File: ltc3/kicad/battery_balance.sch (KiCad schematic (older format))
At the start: 41 parts, among them P701 BATT_MAIN, Q701 SUM110P08-11L, Q702 SUM110P08-11L, Q703 MMBT3904, U701 BQ77PL900

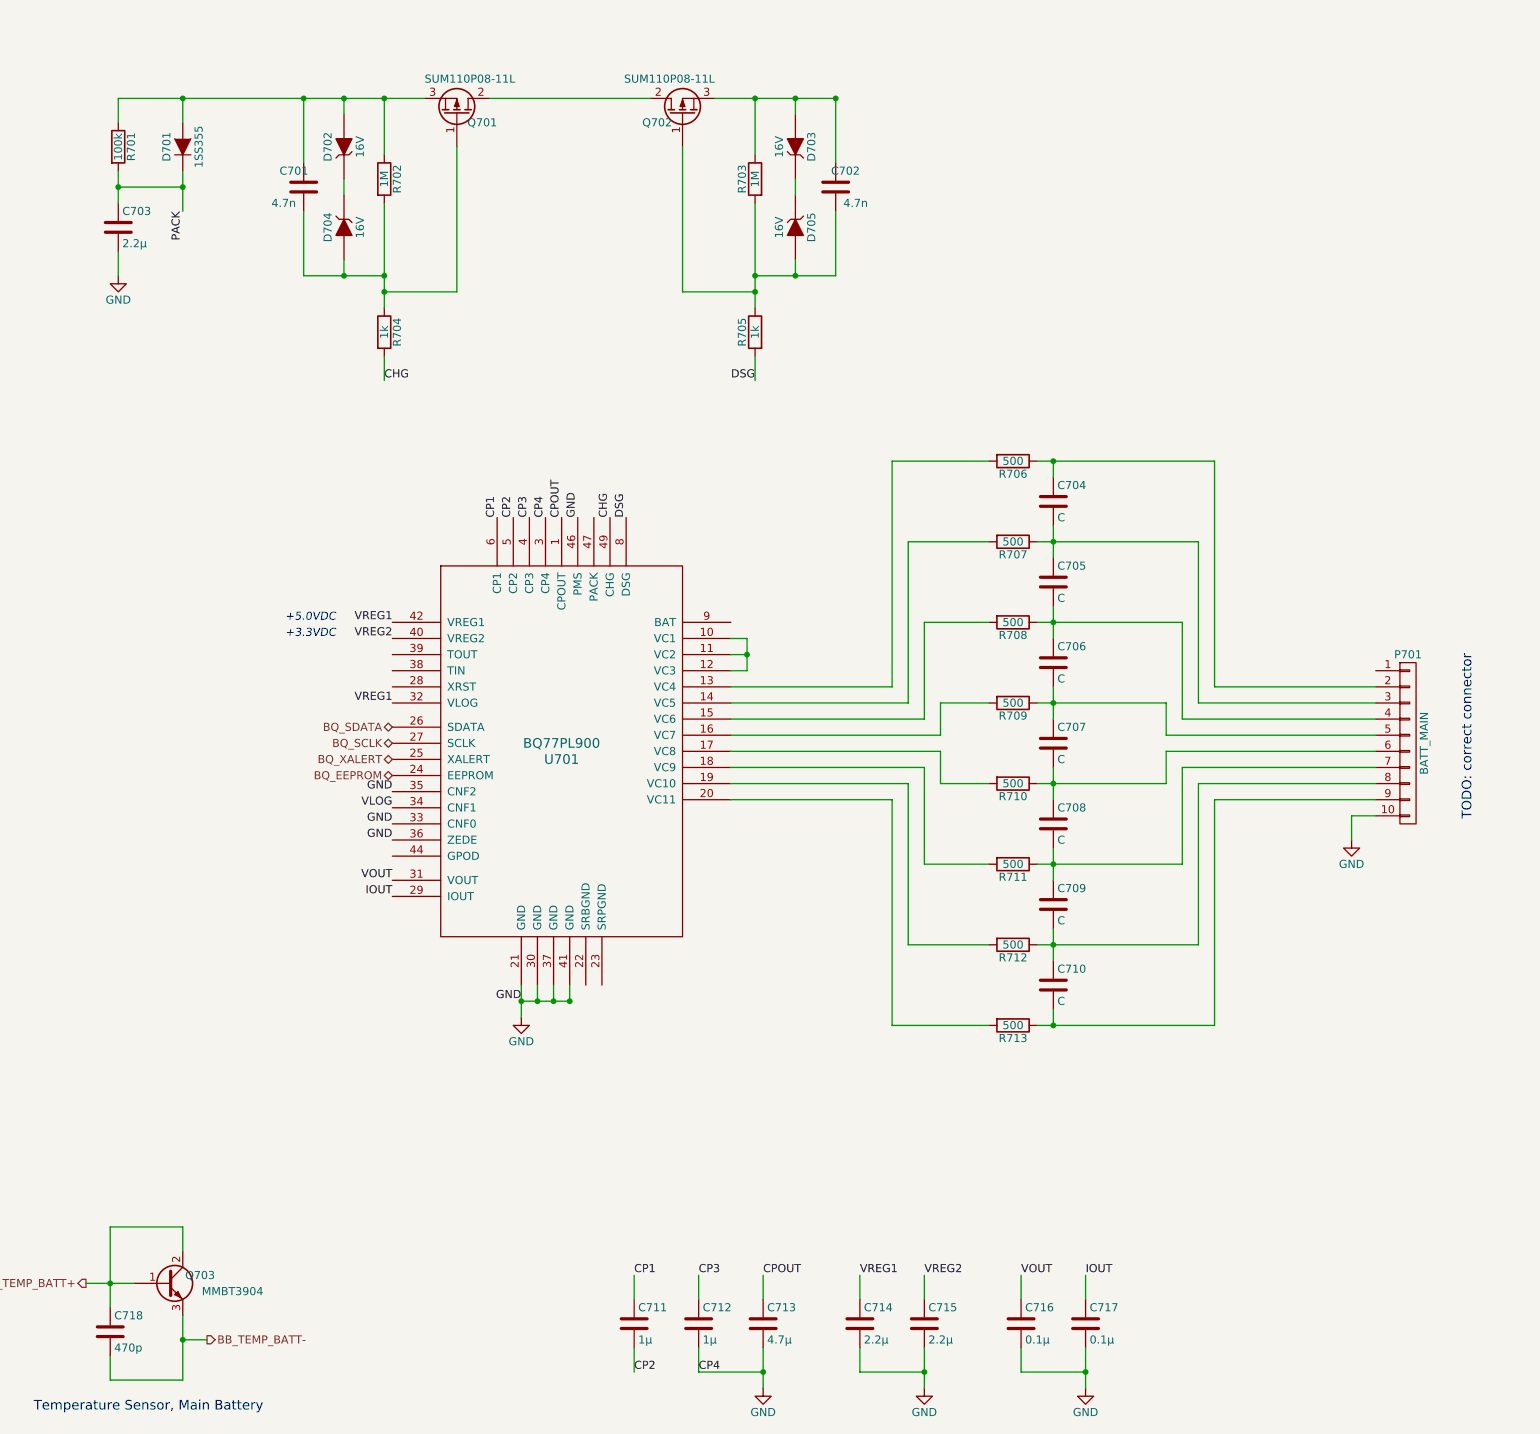
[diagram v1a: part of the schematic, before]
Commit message: LTC3: Reordered schematic sub-sheets; updated PDF export of schematic.
KiCad has an odd habit of ordering a schematic's sub-sheets without
notice.
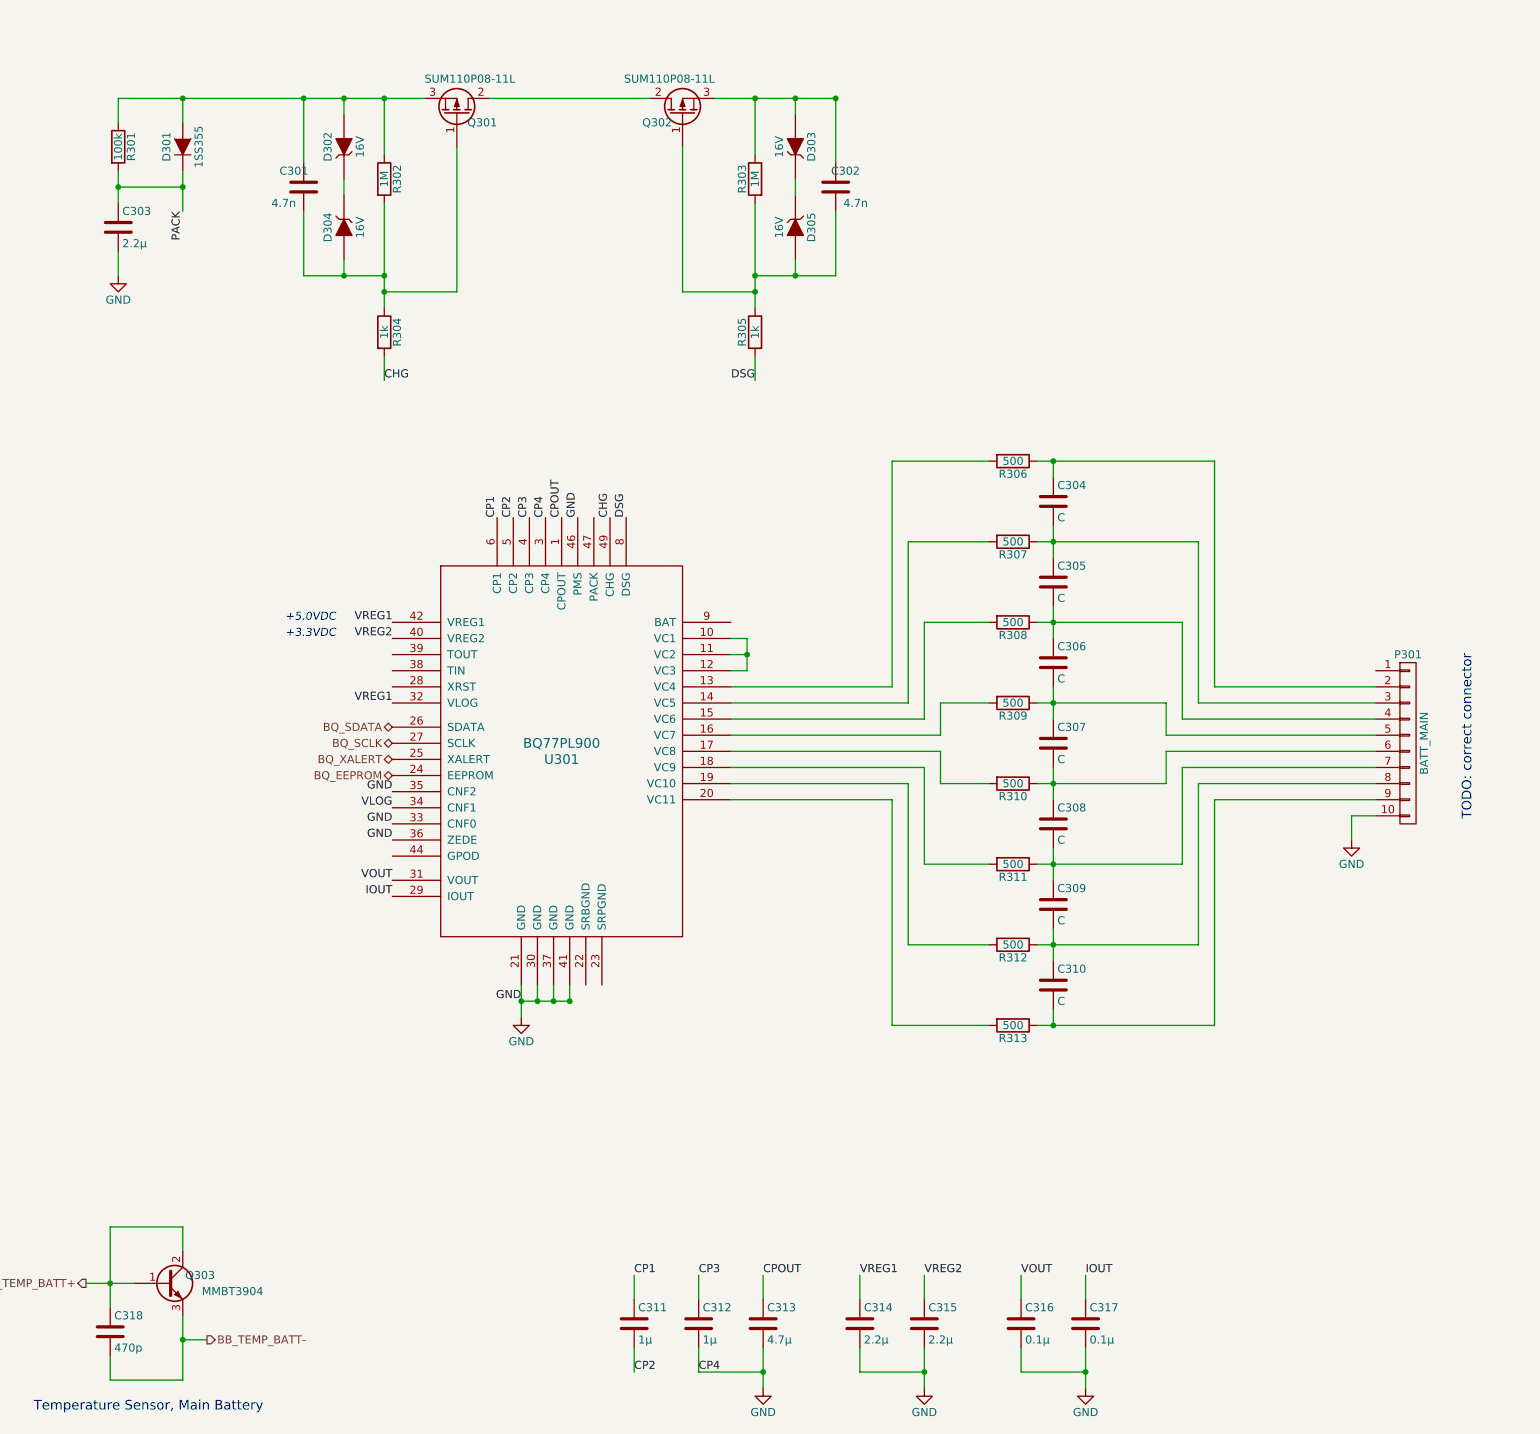
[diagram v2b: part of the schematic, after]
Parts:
- renumbered C701 to C301, C702 to C302, C703 to C303, C704 to C304, C705 to C305, C706 to C306, C707 to C307, C708 to C308, C709 to C309, C710 to C310, C711 to C311, C712 to C312, C713 to C313, C714 to C314, C715 to C315, C716 to C316, C717 to C317, C718 to C318, D701 to D301, D702 to D302, D703 to D303, D704 to D304, D705 to D305, P701 to P301, Q701 to Q301, Q702 to Q302, Q703 to Q303, R701 to R301, R702 to R302, R703 to R303, R704 to R304, R705 to R305, R706 to R306, R707 to R307, R708 to R308, R709 to R309, R710 to R310, R711 to R311, R712 to R312, R713 to R313, U701 to U301

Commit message: LTC3: Cleaned up I2C devices.
Gave each power sub-circuit its own LTC299x sensor.  Charger and
battery pack circuits each get an LTC2990 (quad); DC-DC converter
circuit gets an LTC2991 (octal).

Separate sensor ICs for each sub-circuit allows the chip to be as
close to its sense resistors as possible (and makes for a cleaner
schematic).
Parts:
- removed C318: 470p, symbol C
- removed P301: BATT_MAIN, symbol CONN_01X10
- removed Q303: MMBT3904, symbol Q_NPN_BCE
- added C?: 0.1μ, symbol C
- added C?: 470p, symbol C
- added P?: CONN_BATT_SENSE, symbol CONN_01X08
- added P?: CONN_BATT_MAIN, symbol CONN_01X02
- added Q?: MMBT3904, symbol Q_NPN_BCE
- added R?: R4T, symbol R4T
- added R?: 5k6, symbol R
- added U?: LTC2990, symbol LTC2990
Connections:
- net GND: now also C?.2, P?.2 (P2), U?.5 (GND), U?.9 (ADR1)
- net at U301.9 (BAT): now also C302.1, D303.2 (A), Q302.3 (S), R303.1, R?.2
- net at C304.1, R306.1: now also P?.1 (P1)
- net at C304.2, C305.1, R307.1: now also P?.2 (P2)
- net at C305.2, C306.1, R308.1: now also P?.3 (P3)
- net at C306.2, C307.1, R309.1: now also P?.4 (P4)
- net at C307.2, C308.1, R310.1: now also P?.5 (P5)
- net at C308.2, C309.1, R311.1: now also P?.6 (P6)
- net at C309.2, C310.1, R312.1: now also P?.7 (P7)
- net at C310.2, R313.1: now also P?.8 (P8)
- net VBATT: now reaches C301.1, D301.2 (A), D302.2 (A), Q301.3 (S), R301.1, R302.1
- net BQ_SCLK renamed I2C_CLOCK
- net I2C_CLOCK: now also U?.7 (SDL)
- net BQ_SDATA renamed I2C_DATA
- net I2C_DATA: now also U?.6 (SDA)
- net CHG: no longer names the net of R304.2, U301.49 (CHG)
- net DSG: no longer names the net of R305.2, U301.8 (DSG)
- new net: P?.1 (P1), R?.1
- new net: R?.4, U?.1 (V1)
- new net: R?.3, U?.2 (V2)
- new net: C?.1, Q?.1 (B), Q?.2 (C), U?.3 (V3)
- new net: C?.2, Q?.3 (E), U?.4 (V4)
- new net: R?.2, U?.8 (ADR0)
- new net +5V: C?.1, R?.1, U?.10 (Vcc)
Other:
- note added: "I2C addr 0x9A"
- note added: "QUESTIONS:\n* Leave XRST unconnected (p.35)?\n* Leave GPOD unconnected (p.34)?\n* Are caps on VOUT and IOUT necessary if both outputs\n are disabled (pp.30,33)?\n* Do we need multiple parallel switching FETs?\nTODO:\n* Finish circuit.\nNB: Page references are to the bq datasheet."
- note added: "Temp. Sense, Battery"
- note added: "Voltage, Current, & Temp Sense"
- note removed: "QUESTIONS:\n* Can the bq and/or LT8490's batt temp sensing be\n accessed by the BeagleBone?\n* Leave XRST unconnected (p.35)?\n* Leave GPOD unconnected (p.34)?\n* Are caps on VOUT and IOUT necessary if both outputs\n are disabled (pp.30,33)?\n* Do we need multiple parallel switching FETs?\nTODO:\n* Finish circuit.\nNB: Page references are to the bq datasheet."
- note removed: "TODO: correct connector"
- note removed: "Temperature Sensor, Main Battery"
- moved on the sheet: C301, C302, C303, C304, C305, C306, C307, C308, C309, C310, C311, C312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

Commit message: LTC3: Progress on battery cell balancing schematic.
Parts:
- added C?: 2.2μ, symbol C
- added C?: 10n, symbol C
- added C?: 0.1μ, symbol C
- added D?: 1SS355, symbol D
- added Q? (x2): SUM110P08-11L, symbol Q_PMOS_GDS
- added R?: 100k, symbol R
- added R?: 61k9, symbol R
- added R?: 6k98, symbol R
- added R? (x2): 200, symbol R
- added TH?: 10k, symbol THERMISTOR
- R301: value 100k -> 10k
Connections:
- net PACK is gone; now on an unnamed net: C303.1, D301.1 (K), R301.2
- net VREG1 is gone; now on an unnamed net: C314.1, U301.32 (VLOG), U301.42 (VREG1)
- net GND: now also C?.2, C?.2, R?.2, R?.2, R?.2, TH?.2
- net VBATT: now also Q?.3 (S)
- net at U301.10 (VC1), U301.11 (VC2), U301.12 (VC3): now also R306.2, U301.13 (VC4)
- net at U301.22 (SRBGND): now also C?.1, R?.1
- net at U301.23 (SRPGND): now also C?.2, R?.1
- net at U301.38 (TIN): now also C?.1, R?.1, R?.2, TH?.1
- net at U301.39 (TOUT): now also R?.1
- net at C302.1, D303.2 (A), Q302.3 (S)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: now also D?.2 (A), Q?.3 (S), R?.1; no longer U301.9 (BAT)
- net at C301.2, D304.2 (A), Q301.1 (G)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: now also Q?.1 (G)
- net at Q301.2 (D), Q302.2 (D): now also Q?.2 (D), Q?.2 (D)
- net at C302.2, D305.2 (A), Q302.1 (G)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: now also Q?.1 (G)
- net CP1: no longer names the net of C311.1, U301.6 (CP1)
- net CP2: no longer names the net of C311.2, U301.5 (CP2)
- net CP3: no longer names the net of C312.1, U301.4 (CP3)
- net CPOUT: no longer names the net of C313.1, U301.1 (CPOUT)
- net IOUT: no longer names the net of U301.29 (IOUT)
- net IOUT: now also C316.1; no longer C317.1
- net VLOG: no longer names the net of U301.34 (CNF1)
- net VOUT: no longer names the net of U301.31 (VOUT)
- net VOUT: now also C317.1; no longer C316.1
- net VREG2: no longer names the net of C315.1, U301.40 (VREG2)
- new net: C?.1, D?.1 (K), R?.2, U301.9 (BAT)
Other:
- note added: "NB:\n* Page references are to the bq datasheet.\n* bq77PL900 I2C addr 0x10"
- note added: "QUESTIONS:\n* Leave XRST unconnected (p.35)?\n* Leave GPOD unconnected (p.34)?\n* Are caps on VOUT and IOUT necessary if both outputs\n are disabled (pp.30,33)?\n* Do we need multiple parallel switching FETs?"
- note removed: "QUESTIONS:\n* Leave XRST unconnected (p.35)?\n* Leave GPOD unconnected (p.34)?\n* Are caps on VOUT and IOUT necessary if both outputs\n are disabled (pp.30,33)?\n* Do we need multiple parallel switching FETs?\nTODO:\n* Finish circuit.\nNB: Page references are to the bq datasheet."
- moved on the sheet: C301, C302, C303, C304, C305, C306, C307, C308, C309, C310, C311, C312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

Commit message: LTC3: Minor edits to battery charging, balance sheets.
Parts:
- removed C316, C317: 0.1μ, symbol C
- added R?: 1m, symbol R
- added R?: 1m, symbol R4T
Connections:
- net GND: now also R?.1; no longer P?.2 (P2), R?.2, R?.2
- new net: P?.2 (P2), R?.2
- new net: R?.2, R?.3
- new net: R?.2, R?.4
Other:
- note added: "NB:\n* Page references are to the bq datasheet.\n* bq77PL900 I2C addr 0x10\n\nUNCONNECTED PINS\n* VOUT and IOUT are internally connected to ground\n when disabled (pp. 30, 33).\n* XRST is an open-drain output with an internal\n 3k pull-up to VLOG (p. 35)."
- note removed: "NB:\n* Page references are to the bq datasheet.\n* bq77PL900 I2C addr 0x10"
- moved on the sheet: C311, C312, C313, P?, R?

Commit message: LTC3: More work on battery protection/balance schematic.
1. Created custom schematic symbols for switching FETs.
2. Added "zero-volt charging" circuitry.
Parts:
- removed C304, C305, C306, C307, C308, C309, C310: C, symbol C
- removed Q301, Q302, Q? (x2): SUM110P08-11L, symbol Q_PMOS_GDS
- removed R?: 1m, symbol R
- added BT?: Battery, symbol Battery
- added C? (x7): 0.1μ, symbol C
- added Q? (x4): SUM110P08-11, TO-263, symbol SUM110P08-11
- added Q?: NDS9407, SO-8, symbol NDS9407
- added R?: 1k78, symbol R
- added R?: 390k, symbol R
- added R?: 820k, symbol R
- gave numbers to parts that had none: 1
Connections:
- net VBATT: now also Q?.3, Q?.3
- net at U301.44 (GPOD): now also R?.2
- net at P?.1 (P1), R306.1: now also C?.1
- net at P?.2 (P2), R307.1: now also C?.1, C?.2
- net at P?.3 (P3), R308.1: now also C?.1, C?.2
- net at P?.4 (P4), R309.1: now also C?.1, C?.2
- net at P?.5 (P5), R310.1: now also C?.1, C?.2
- net at P?.6 (P6), R311.1: now also C?.1, C?.2
- net at P?.7 (P7), R312.1: now also C?.1, C?.2
- net at P?.8 (P8), R313.1: now also C?.2
- net at C301.2, D304.2 (A), R302.2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: now also Q?.1, Q?.1
- net at C302.2, D305.2 (A), R303.2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: now also Q?.1, Q?.1
- net at 30m.2, C302.1, D303.2 (A)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: now also Q?.3, Q?.3
- new net: Q?.5, Q?.6, Q?.7, Q?.8, R?.1
- new net: Q?.2, Q?.2, Q?.2, Q?.2, R?.2
- new net: Q?.1, Q?.2, Q?.3, R?.1
- new net: Q?.4, R?.1, R?.2
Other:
- note added: "NB: Optional second pair of FETs."
- note added: "TODO:\n* Clean up zero-battery-volt charging circuitry.\n* Add symbol representing off-board battery pack.\n\nQUESTIONS:\n* Leave XRST unconnected (p.35)?\n* Leave GPOD unconnected (p.34)?\n* Are caps on VOUT and IOUT necessary if both outputs\n are disabled (pp.30,33)?"
- note removed: "QUESTIONS:\n* Leave XRST unconnected (p.35)?\n* Leave GPOD unconnected (p.34)?\n* Are caps on VOUT and IOUT necessary if both outputs\n are disabled (pp.30,33)?\n* Do we need multiple parallel switching FETs?"

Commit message: LTC3: Re-annotated schematic; updated PDF.
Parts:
- gave numbers to parts that had none: 34
- renumbered 30m to 30m301, C301 to C303, C302 to C304, C303 to C305, C313 to C307, C312 to C308, C311 to C309, C314 to C313, C315 to C314, D304 to D305, D305 to D306, R301 to R305, R302 to R306, R303 to R307, R304 to R309, R305 to R310, R306 to R311, R307 to R312, R308 to R313, R309 to R315, R310 to R316, R311 to R318, R312 to R319, R313 to R320, U301 to U302

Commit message: LTC3: Final clean-up of battery protection schematic.
Until the next clean-up.
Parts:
- removed BT301: Battery, symbol Battery
- added PHNTM301: ~, symbol CONN_01X02
- added PHNTM302, PHNTM303, PHNTM305, PHNTM306, PHNTM307, PHNTM308, PHNTM309, PHNTM310: ~, symbol Battery
- added PHNTM304: ~, symbol CONN_01X08
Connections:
- new net: PHNTM301.1 (P1), PHNTM302.1, PHNTM304.1 (P1)
- new net: PHNTM302.2, PHNTM303.1, PHNTM304.2 (P2)
- new net: PHNTM303.2, PHNTM304.3 (P3), PHNTM305.1
- new net: PHNTM304.4 (P4), PHNTM305.2, PHNTM306.1
- new net: PHNTM304.5 (P5), PHNTM306.2, PHNTM307.1
- new net: PHNTM304.6 (P6), PHNTM307.2, PHNTM308.1
- new net: PHNTM304.7 (P7), PHNTM308.2, PHNTM309.1
- new net: PHNTM304.8 (P8), PHNTM309.2, PHNTM310.1
- new net: PHNTM301.2 (P2), PHNTM310.2
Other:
- note added: "Main Battery (off-board)"
- note added: "NB:\n* Page references are to the bq datasheet.\n* "PHNTM" components represent off-board devices.\n Do not assign footprints to these components.\n* bq77PL900 I2C addr is 0x10 (p.38).\n\nUNCONNECTED PINS\n* VOUT and IOUT are internally connected to ground\n when disabled (pp. 30, 33).\n* XRST is an open-drain output with an internal\n 3k pull-up to VLOG (p. 35)."
- note added: "QUESTIONS:\n* Leave XRST (open drain) unconnected (p.35)?\n* Are caps on VOUT and IOUT necessary if both\noutputs are disabled (pp.30,33)?"
- note removed: "NB: Optional second pair of FETs."
- note removed: "NB:\n* Page references are to the bq datasheet.\n* bq77PL900 I2C addr 0x10\n\nUNCONNECTED PINS\n* VOUT and IOUT are internally connected to ground\n when disabled (pp. 30, 33).\n* XRST is an open-drain output with an internal\n 3k pull-up to VLOG (p. 35)."
- note removed: "TODO:\n* Clean up zero-battery-volt charging circuitry.\n* Add symbol representing off-board battery pack.\n\nQUESTIONS:\n* Leave XRST unconnected (p.35)?\n* Leave GPOD unconnected (p.34)?\n* Are caps on VOUT and IOUT necessary if both outputs\n are disabled (pp.30,33)?"
- moved on the sheet: Q301, R302, R303, R304
